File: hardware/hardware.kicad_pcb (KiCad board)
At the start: 4 copper layers, 55 parts, among them J1 JST-PH, J2 SWD Debug, J3 COMPANION, J4 CAM PWR, Q1 AO3401A, SW1 SW_Push, U1 TPS562202S, U2 TPS562202S, U3 STM32G071KBUxN, U4 INA226

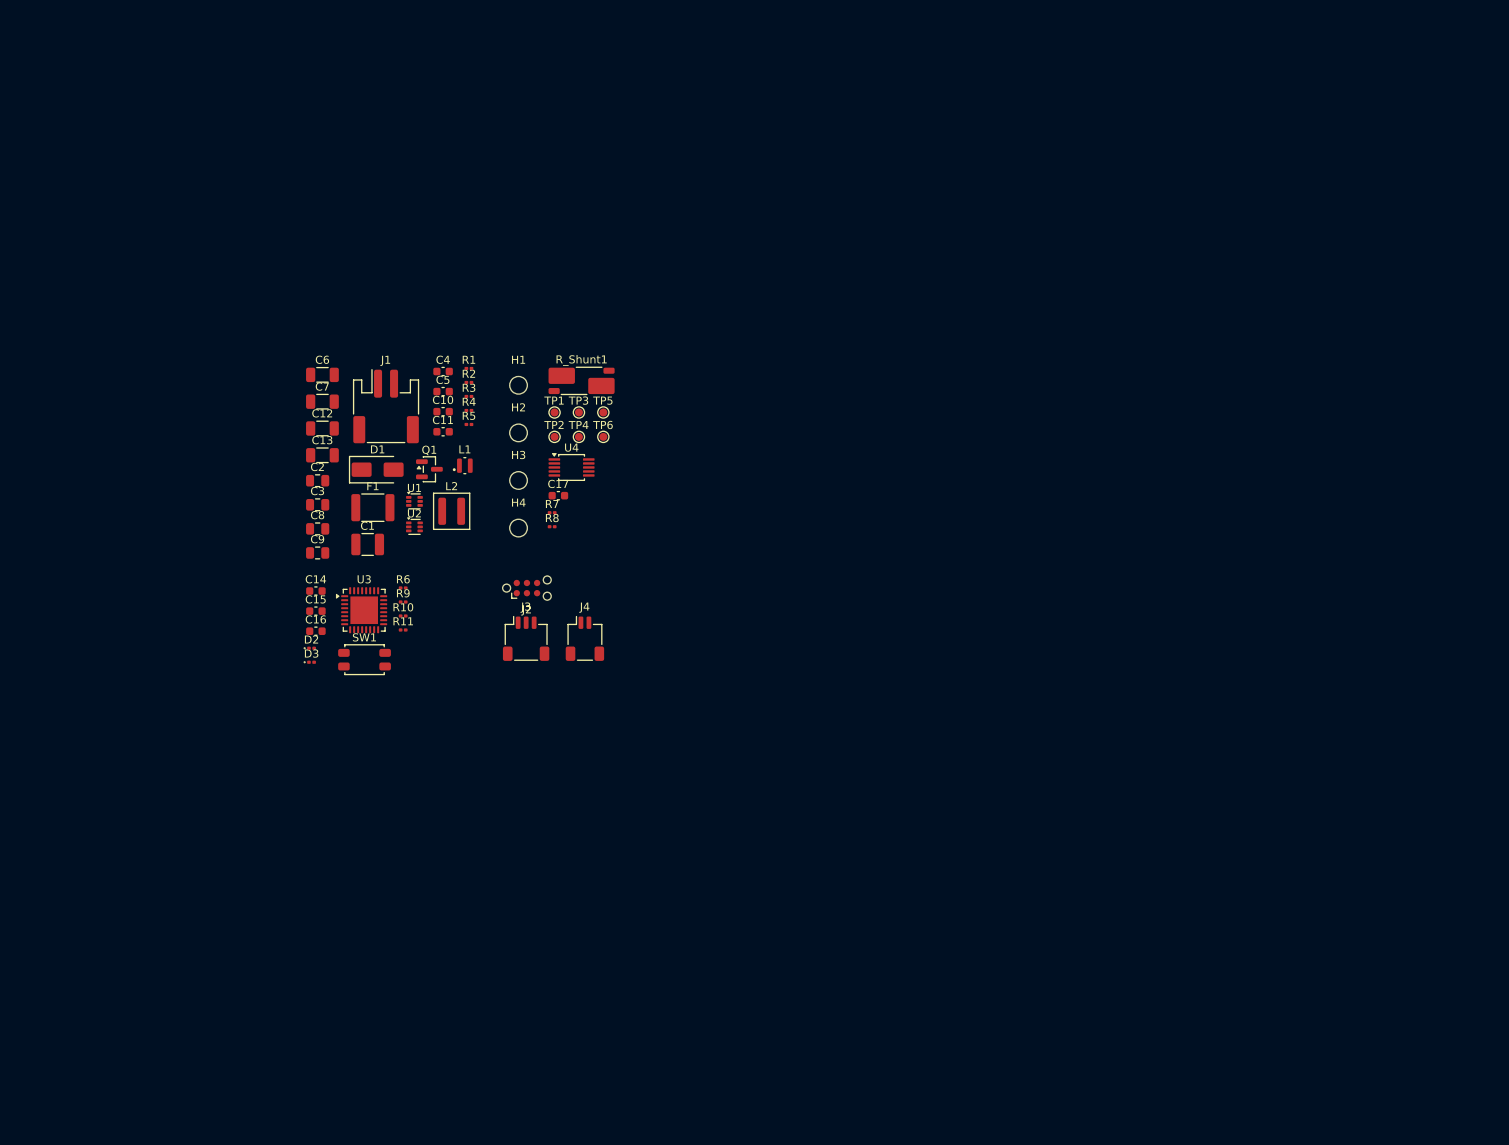
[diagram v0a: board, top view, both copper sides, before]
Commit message: Short Circuit Fix
There were root label connections that short circuited some of the pins, so they were removed and properly addressed
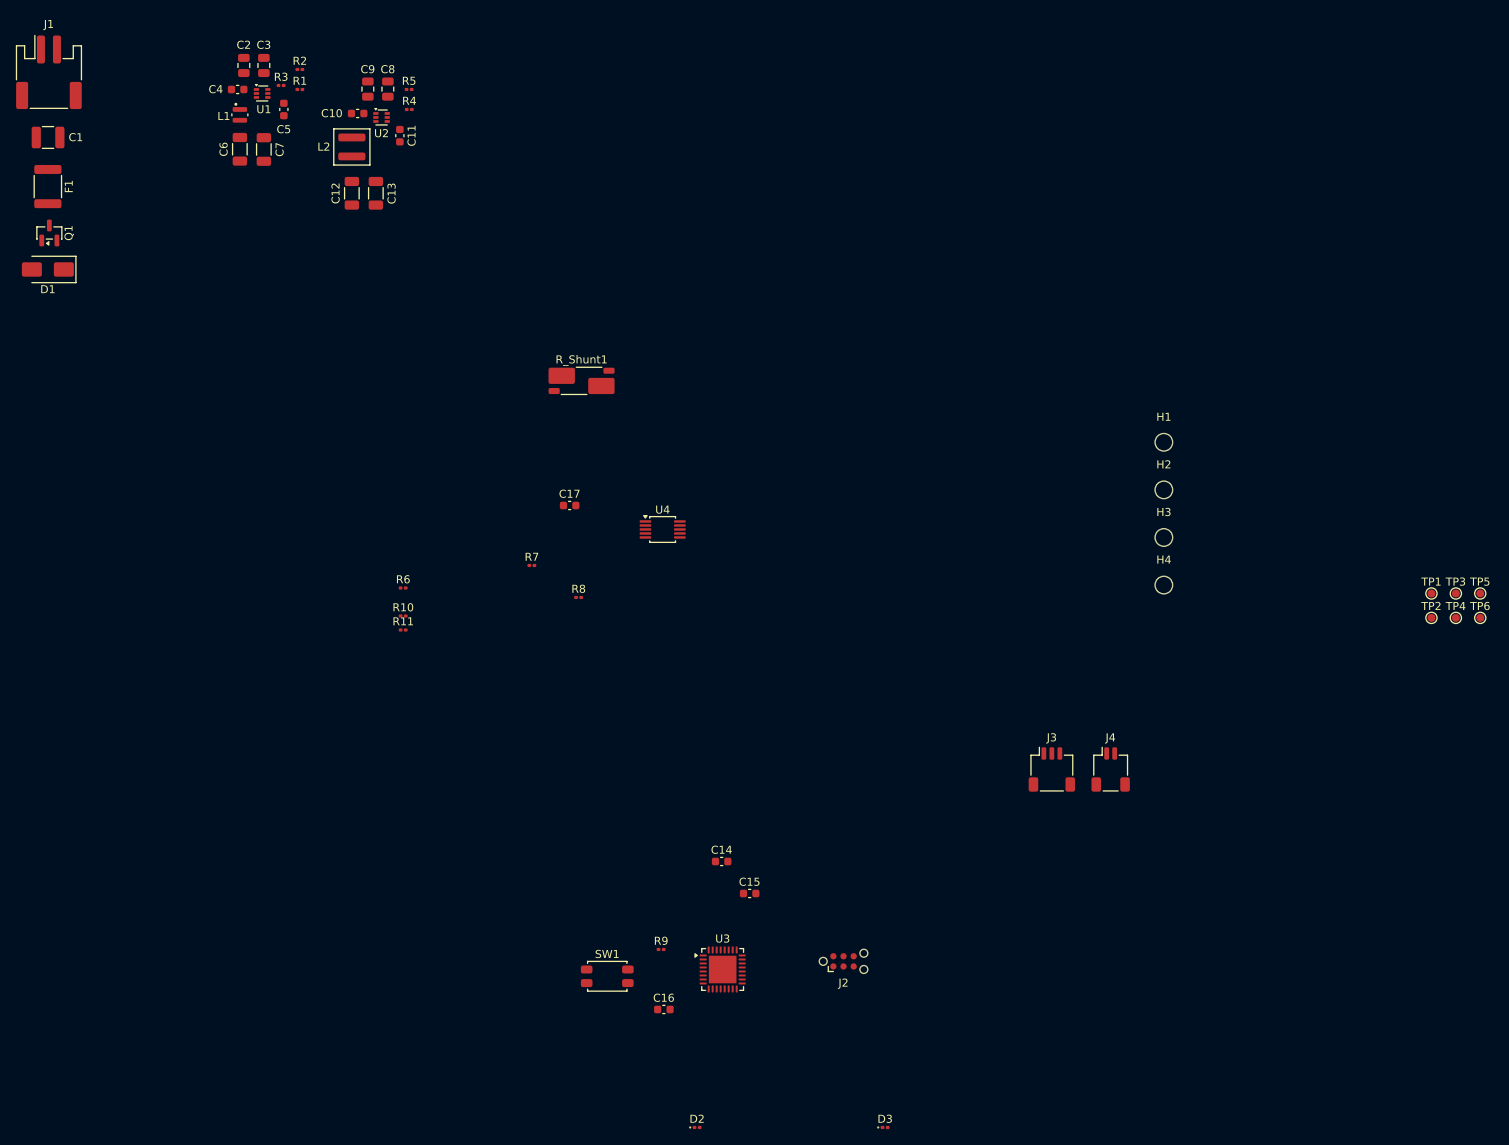
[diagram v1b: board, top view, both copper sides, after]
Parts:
- moved TP5 111.9 mm to (207.6, 87.0)
- moved TP6 111.9 mm to (207.6, 90.0)
- moved TP1 111.9 mm to (201.4, 87.0)
- moved TP2 111.9 mm to (201.4, 90.0)
- moved TP3 111.9 mm to (204.5, 87.0)
- moved TP4 111.9 mm to (204.5, 90.0)
- moved D3 92.3 mm to (133.2, 153.8)
- moved H1 81.0 mm to (168.0, 68.1)
- moved H2 81.0 mm to (168.0, 74.0)
- moved H3 81.0 mm to (168.0, 80.0)
- moved H4 81.0 mm to (168.0, 86.0)
- moved D2 76.9 mm to (109.7, 153.8)
- moved J3 67.7 mm to (154.0, 109.0)
- moved J4 67.7 mm to (161.3, 109.0)
- moved C15 64.7 mm to (116.2, 124.5)
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
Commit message: Completed PCB Layout
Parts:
- moved F1 130.3 mm to (153.2, 73.8)
- moved J1 128.4 mm to (151.0, 60.9), turned to 180 degrees
- moved C1 128.0 mm to (147.8, 76.5), turned to 180 degrees
- moved D1 123.6 mm to (150.2, 68.0)
- moved Q1 123.2 mm to (148.0, 72.5)
- moved C9 103.6 mm to (152.6, 84.5), turned to 0 degrees
- moved C8 103.1 mm to (152.6, 87.0), turned to 0 degrees
- moved R5 102.6 mm to (152.5, 89.7), turned to -90 degrees
- moved C2 101.4 mm to (142.5, 68.8), turned to -90 degrees
- moved C4 100.2 mm to (143.3, 65.8), turned to 0 degrees
- moved C10 99.7 mm to (149.5, 83.2), turned to 90 degrees
- moved R4 99.1 mm to (150.0, 89.7), turned to -90 degrees
- moved U2 98.3 mm to (149.0, 86.2), turned to -90 degrees
- moved L1 97.2 mm to (143.0, 62.6), turned to 90 degrees
- moved C3 97.1 mm to (140.0, 68.8), turned to -90 degrees
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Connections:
- C1 pad 1: /Connectors_Comms/3V3 -> /Current_Sense/VBAT_PROT
- C10 pad 1: /Connectors_Comms/3V3 -> /Current_Sense/VBAT_PROT
- C2 pad 1: /Connectors_Comms/3V3 -> /Current_Sense/VBAT_PROT
- C3 pad 1: /Connectors_Comms/3V3 -> /Current_Sense/VBAT_PROT
- C4 pad 1: /Connectors_Comms/3V3 -> /Current_Sense/VBAT_PROT
- C8 pad 1: /Connectors_Comms/3V3 -> /Current_Sense/VBAT_PROT
- C9 pad 1: /Connectors_Comms/3V3 -> /Current_Sense/VBAT_PROT
- D1 pad 1: /Connectors_Comms/3V3 -> /Current_Sense/VBAT_RAW
- F1 pad 1: /Connectors_Comms/3V3 -> /Current_Sense/VBAT_RAW
- J1 pad 1: /Connectors_Comms/3V3 -> /Current_Sense/VBAT_RAW
- Q1 pad 2: /Connectors_Comms/3V3 -> /Current_Sense/VBAT_PROT
- R3 pad 1: /Connectors_Comms/3V3 -> /Current_Sense/VBAT_PROT
- TP1 pad 1: /Connectors_Comms/3V3 -> /Current_Sense/VBAT_RAW
- TP2 pad 1: /Connectors_Comms/3V3 -> /Current_Sense/VBAT_PROT
- U1 pad 1: /Connectors_Comms/3V3 -> /Current_Sense/VBAT_PROT
- U2 pad 1: /Connectors_Comms/3V3 -> /Current_Sense/VBAT_PROT
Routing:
- added copper zone on In1.Cu, net GND
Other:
- board outline added: 44.2 x 37 mm

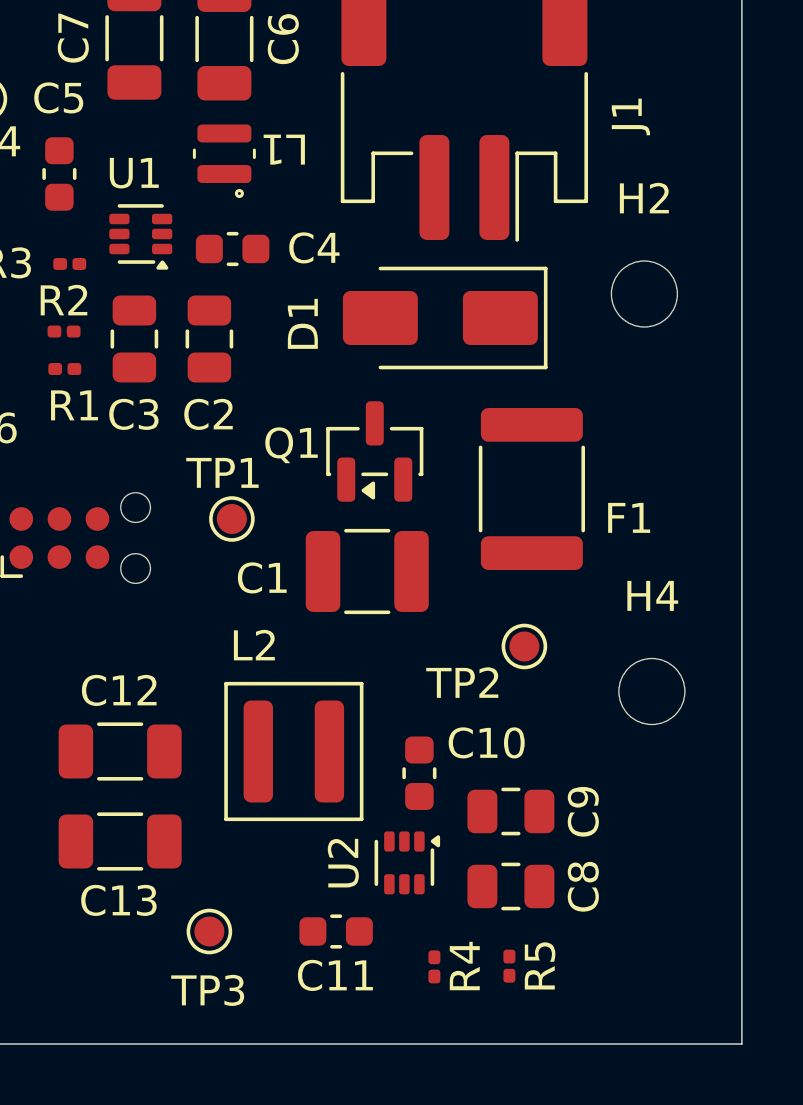
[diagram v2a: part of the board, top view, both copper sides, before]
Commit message: Added missing 3d models
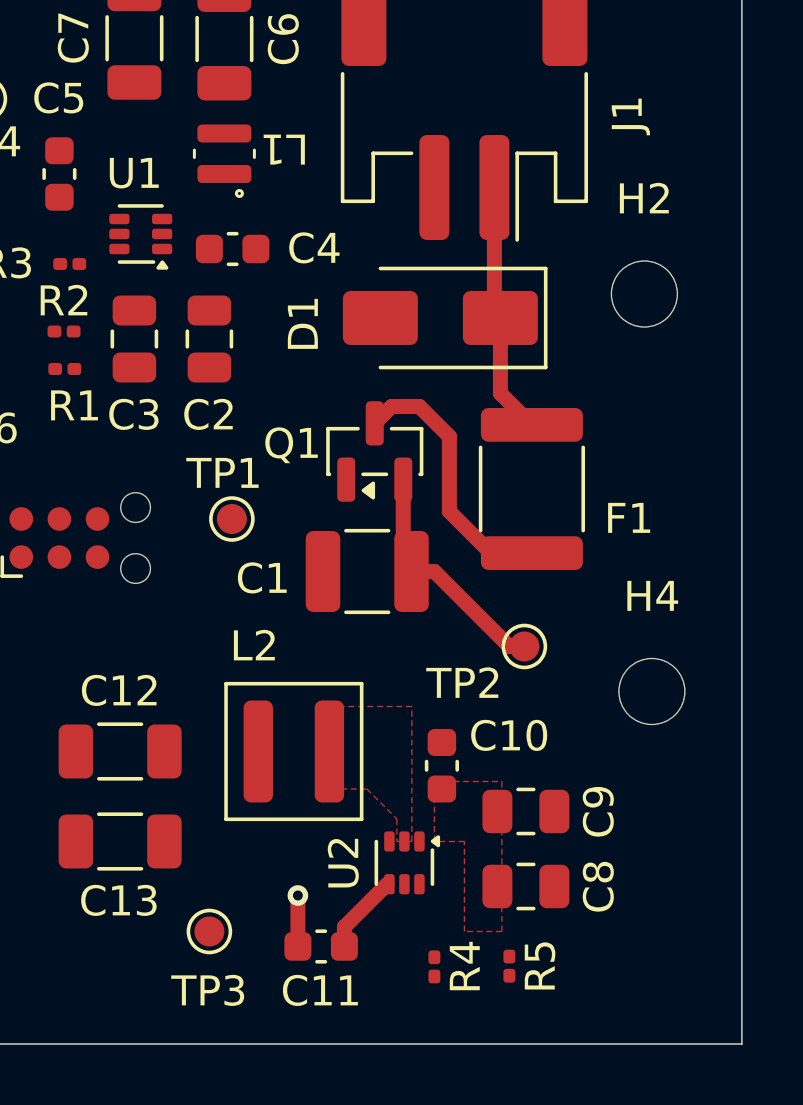
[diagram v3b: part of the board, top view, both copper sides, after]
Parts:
- moved C10 0.79 mm to (150.2, 83.0)
- moved C11 0.71 mm to (146.2, 89.0)
- moved C8 0.50 mm to (153.1, 87.0)
- moved C9 0.50 mm to (153.1, 84.5)
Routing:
- net Net-(Q1-D): track 0.00 -> 8.96 mm
- net /Current_Sense/VBAT_RAW: track 0.00 -> 8.15 mm
- net /Current_Sense/VBAT_PROT: track 0.00 -> 7.97 mm
- net Net-(U2-VBST): track 0.00 -> 2.67 mm
- net Net-(U2-SW): track 0.00 -> 1.70 mm, vias 0 -> 1
- added copper zone on F.Cu, net /Current_Sense/VBAT_PROT
- added copper zone on F.Cu, net Net-(U2-SW)
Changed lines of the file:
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@@
 	(footprint "Capacitor_SMD:C_0805_2012Metric"
 		(layer "F.Cu")
-		(at 152.55 84.5)
+		(at 153.05 84.5)
 		(descr "Capacitor SMD 0805 (2012 Metric), square (rectangular) end terminal, IPC-7351 nominal, (Body size source: IPC-SM-782 page 76, https://www.pcb-3d.com/wordpress/wp-content/uploads/ipc-sm-782a_amendment_1_and_2.pdf, https://docs.google.com/spreadsheets/d/1BsfQQcO9C6DZCsRaXUlFlo91Tg2WpOkGARC1WS5S8t0/edit?usp=sharing)")
 		(tags "capacitor")
@@
 	(footprint "Capacitor_SMD:C_0603_1608Metric"
 		(layer "F.Cu")
-		(at 149.5 83.225 90)
+		(at 150.25 82.975 90)
 		(descr "Capacitor SMD 0603 (1608 Metric), square (rectangular) end terminal, IPC-7351 nominal, (Body size source: IPC-SM-782 page 76, https://www.pcb-3d.com/wordpress/wp-content/uploads/ipc-sm-782a_amendment_1_and_2.pdf)")
 		(tags "capacitor")
@@
 		)
 		(embedded_fonts no)
-		(model "${KICAD10_3DMODEL_DIR}/Resistor_SMD.3dshapes/R_Shunt_Vishay_WSK2512_6332Metric_T2.21mm.step"
+		(model "${KIPRJMOD}/libraries/WSK2512 (0.005 to 0.2).stp"
 			(offset
 				(xyz 0 0 0)
@@
 	(footprint "Capacitor_SMD:C_0603_1608Metric"
 		(layer "F.Cu")
-		(at 146.725 88.5 180)
+		(at 146.225 89 180)
 		(descr "Capacitor SMD 0603 (1608 Metric), square (rectangular) end terminal, IPC-7351 nominal, (Body size source: IPC-SM-782 page 76, https://www.pcb-3d.com/wordpress/wp-content/uploads/ipc-sm-782a_amendment_1_and_2.pdf)")
 		(tags "capacitor")
@@
 		)
 		(embedded_fonts no)
-		(model "${KICAD10_3DMODEL_DIR}/Connector_JST.3dshapes/JST_PH_S2B-PH-SM4-TB_1x02-1MP_P2.00mm_Horizontal.step"
+		(model "${KIPRJMOD}/libraries/S2B-PH-SM4-TB.step"
 			(offset
-				(xyz 0 0 0)
+				(xyz 0 -4.5 0)
 			)
 			(scale
@@
 			)
 			(rotate
-				(xyz 0 0 0)
+				(xyz -90 -0 -0)
 			)
 		)
@@
 	(footprint "Capacitor_SMD:C_0805_2012Metric"
 		(layer "F.Cu")
-		(at 152.55 87)
+		(at 153.05 87)
 		(descr "Capacitor SMD 0805 (2012 Metric), square (rectangular) end terminal, IPC-7351 nominal, (Body size source: IPC-SM-782 page 76, https://www.pcb-3d.com/wordpress/wp-content/uploads/ipc-sm-782a_amendment_1_and_2.pdf, https://docs.google.com/spreadsheets/d/1BsfQQcO9C6DZCsRaXUlFlo91Tg2WpOkGARC1WS5S8t0/edit?usp=sharing)")
 		(tags "capacitor")
@@
 		(layer "Edge.Cuts")
 	)
+	(segment
+		(start 145.45 87.3)
+		(end 145.45 89)
+		(width 0.5)
+		(layer "F.Cu")
+		(net "Net-(U2-SW)")
+	)
+	(via
+		(at 145.45 87.3)
+		(size 0.6858)
+		(drill 0.3302)
+		(layers "F.Cu" "B.Cu")
+		(net "Net-(U2-SW)")
+	)
+	(segment
+		(start 148.9625 76.225)
+		(end 149.2375 76.5)
+		(width 0.5)
+		(layer "F.Cu")
+		(net "/Current_Sense/VBAT_PROT")
+	)
+	(segment
+		(start 148.9625 73.4375)
+		(end 148.9625 76.225)
+		(width 0.5)
+		(layer "F.Cu")
+		(net "/Current_Sense/VBAT_PROT")
+	)
+	(segment
+		(start 152.5 79)
+		(end 153 79)
+		(width 0.5)
+		(layer "F.Cu")
+		(net "/Current_Sense/VBAT_PROT")
+	)
+	(segment
+		(start 149.2375 76.5)
+		(end 150 76.5)
+		(width 0.5)
+		(layer "F.Cu")
+		(net "/Current_Sense/VBAT_PROT")
+	)
+	(segment
+		(start 150 76.5)
+		(end 152.5 79)
+		(width 0.5)
+		(layer "F.Cu")
+		(net "/Current_Sense/VBAT_PROT")
+	)
+	(segment
+		(start 152.2 68.05)
+		(end 152.2 70.5625)
+		(width 0.5)
+		(layer "F.Cu")
+		(net "/Current_Sense/VBAT_RAW")
+	)
+	(segment
+		(start 152 63.7)
+		(end 152 67.85)
+		(width 0.5)
+		(layer "F.Cu")
+		(net "/Current_Sense/VBAT_RAW")
+	)
+	(segment
+		(start 152.2 70.5625)
+		(end 153.25 71.6125)
+		(width 0.5)
+		(layer "F.Cu")
+		(net "/Current_Sense/VBAT_RAW")
+	)
+	(segment
+		(start 147 89)
+		(end 147 88.35)
+		(width 0.5)
+		(layer "F.Cu")
+		(net "Net-(U2-VBST)")
+	)
+	(segment
+		(start 147 88.35)
+		(end 148.425 86.925)
+		(width 0.5)
+		(layer "F.Cu")
+		(net "Net-(U2-VBST)")
+	)
+	(segment
+		(start 148.0125 71.5625)
+		(end 148.575 71)
+		(width 0.5)
+		(layer "F.Cu")
+		(net "Net-(Q1-D)")
+	)
+	(segment
+		(start 149.5 71)
+		(end 150.5 72)
+		(width 0.5)
+		(layer "F.Cu")
+		(net "Net-(Q1-D)")
+	)
+	(segment
+		(start 150.5 74.5)
+		(end 151.8875 75.8875)
+		(width 0.5)
+		(layer "F.Cu")
+		(net "Net-(Q1-D)")
+	)
+	(segment
+		(start 148.575 71)
+		(end 149.5 71)
+		(width 0.5)
+		(layer "F.Cu")
+		(net "Net-(Q1-D)")
+	)
+	(segment
+		(start 150.5 72)
+		(end 150.5 74.5)
+		(width 0.5)
+		(layer "F.Cu")
+		(net "Net-(Q1-D)")
+	)
+	(segment
+		(start 151.8875 75.8875)
+		(end 153.25 75.8875)
+		(width 0.5)
+		(layer "F.Cu")
+		(net "Net-(Q1-D)")
+	)
+	(segment
+		(start 149.5 86.925)
+		(end 149.5 87)
+		(width 0.25)
+		(layer "F.Cu")
+		(net "Net-(U2-VFB)")
+	)
+	(zone
+		(net "/Current_Sense/VBAT_PROT")
+		(layer "F.Cu")
+		(hatch edge 0.5)
+		(priority 2)
+		(connect_pads yes
+			(clearance 0.5)
+		)
+		(min_thickness 0.25)
+		(fill
+			(thermal_gap 0.5)
+			(thermal_bridge_width 0.5)
+			(island_removal_mode 0)
+		)
+		(polygon
+			(pts
+				(xy 150 85.5) (xy 150 83.5) (xy 152.25 83.5) (xy 152.25 88.5) (xy 151 88.5) (xy 151 85.5)
+			)
+		)
+	)
+	(zone
+		(net "Net-(U2-SW)")
+		(layer "F.Cu")
+		(hatch edge 0.5)
+		(priority 1)
+		(connect_pads yes
+			(clearance 0.5)
+		)
+		(min_thickness 0.25)
+		(fill
+			(thermal_gap 0.5)
+			(thermal_bridge_width 0.5)
+			(island_removal_mode 0)
+		)
+		(polygon
+			(pts
+				(xy 149.25 85.5) (xy 149.25 81) (xy 146.25 81) (xy 146.25 83.75) (xy 147.75 83.75) (xy 148.75 84.75)
+				(xy 148.75 85.5)
+			)
+		)
+	)
 	(zone
